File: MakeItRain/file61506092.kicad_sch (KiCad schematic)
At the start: 12 parts, among them Q10 2N7000, Q11 2N7000, Q12 IRF9Z34NPBF

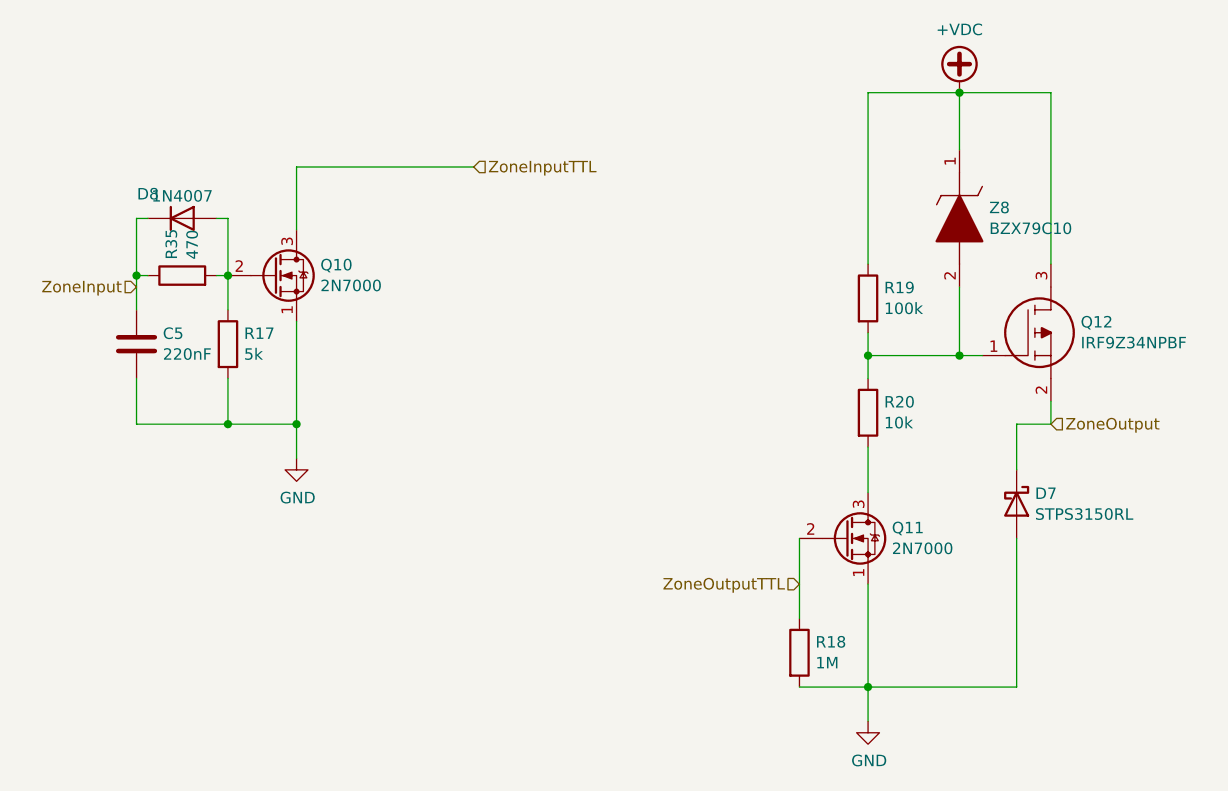
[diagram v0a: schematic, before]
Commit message: upgrading the project to KiCAD 7
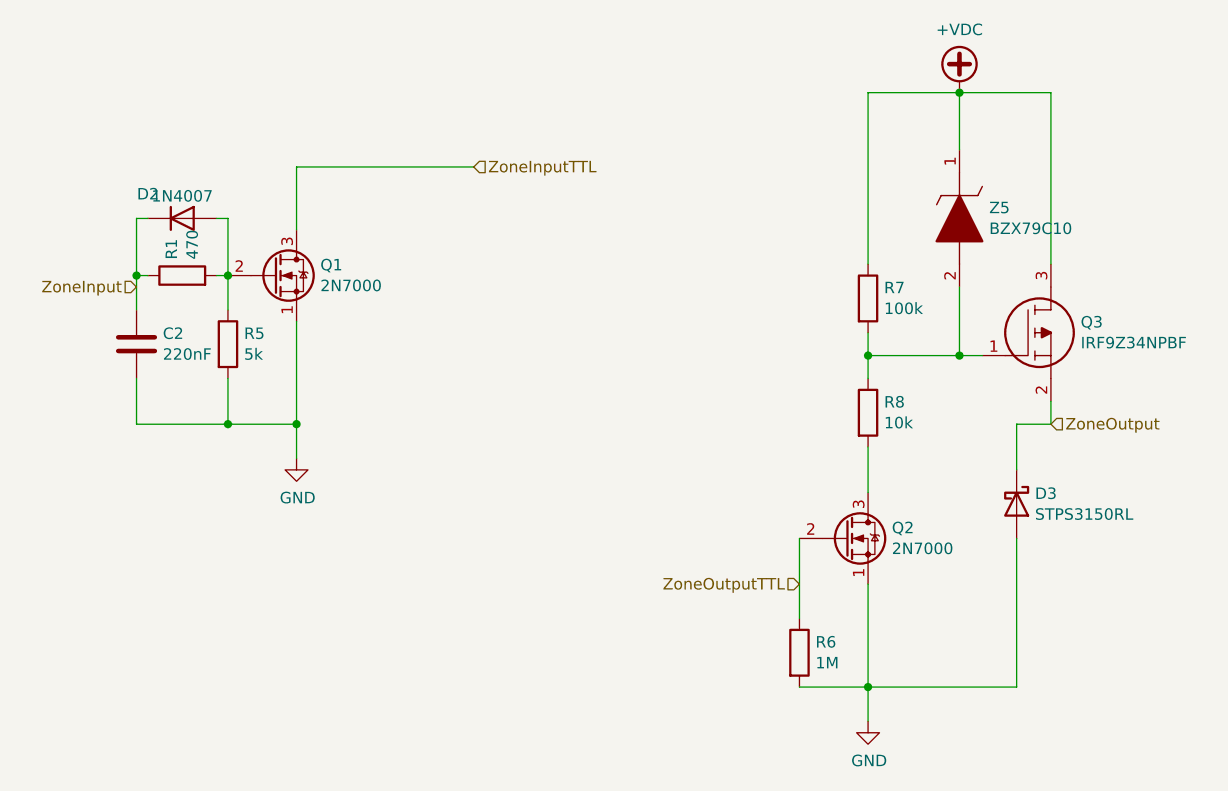
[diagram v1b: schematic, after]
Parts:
- renumbered C5 to C2, D8 to D2, D7 to D3, Q10 to Q1, Q11 to Q2, Q12 to Q3, R35 to R1, R17 to R5, R18 to R6, R19 to R7, R20 to R8, Z8 to Z5

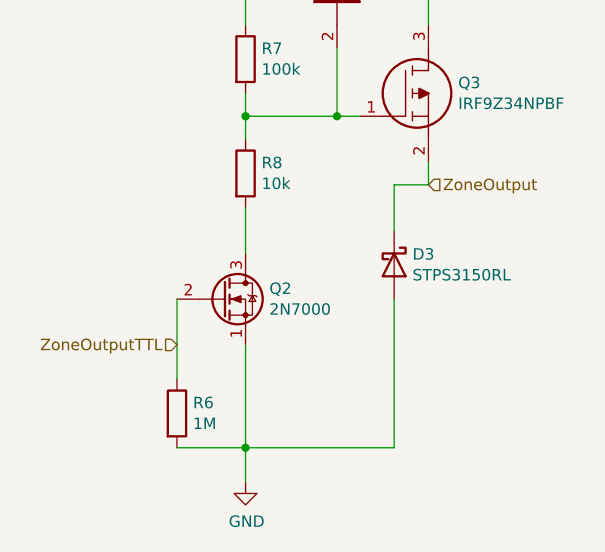
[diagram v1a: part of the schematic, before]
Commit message: WIP - Pre Re-Routing and other Tweaks.
* Removed SMD package for the MCP23008
* removed routings to fix the routes for I2C bus
* flipped rx/tx with SDA/SCL on the expansion port to make routing easier.
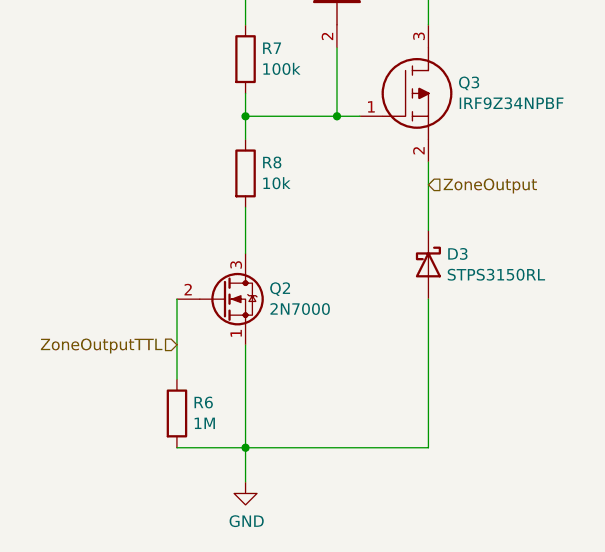
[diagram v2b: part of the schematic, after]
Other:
- moved on the sheet: D3
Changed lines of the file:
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@@
     (stroke (width 0) (type default))
   )
-  (wire (pts (xy 142.24 105.41) (xy 142.24 121.92))
+  (wire (pts (xy 146.05 105.41) (xy 146.05 121.92))
     (stroke (width 0) (type default))
   )
@@
     (stroke (width 0) (type default))
   )
-  (wire (pts (xy 142.24 121.92) (xy 125.73 121.92))
-    (stroke (width 0) (type default))
-  )
-  (wire (pts (xy 142.24 97.79) (xy 142.24 92.71))
+  (wire (pts (xy 146.05 121.92) (xy 125.73 121.92))
     (stroke (width 0) (type default))
   )
@@
     (stroke (width 0) (type default))
   )
-  (wire (pts (xy 142.24 92.71) (xy 146.05 92.71))
-    (stroke (width 0) (type default))
-  )
   (wire (pts (xy 54.61 92.71) (xy 62.23 92.71))
     (stroke (width 0) (type default))
   )
-  (wire (pts (xy 146.05 92.71) (xy 146.05 90.17))
+  (wire (pts (xy 146.05 90.17) (xy 146.05 97.79))
     (stroke (width 0) (type default))
   )
@@
     )
   )
-  (symbol (lib_id "Device:D_Schottky") (at 142.24 101.6 270) (unit 1)
-    (in_bom yes) (on_board yes) (dnp no)
-    (property "Reference" "D3" (at 144.272 100.4316 90)
-      (effects (font (size 1.27 1.27)) (justify left))
-    )
-    (property "Value" "STPS3150RL" (at 144.272 102.743 90)
-      (effects (font (size 1.27 1.27)) (justify left))
-    )
-    (property "Footprint" "Diode_THT:D_DO-201_P15.24mm_Horizontal" (at 142.24 101.6 0)
-      (effects (font (size 1.27 1.27)) hide)
-    )
-    (property "Datasheet" "~" (at 142.24 101.6 0)
-      (effects (font (size 1.27 1.27)) hide)
-    )
+  (symbol (lib_id "Device:D_Schottky") (at 146.05 101.6 270) (unit 1)
+    (in_bom yes) (on_board yes) (dnp no)
+    (property "Reference" "D3" (at 148.082 100.4316 90)
+      (effects (font (size 1.27 1.27)) (justify left))
+    )
+    (property "Value" "STPS3150RL" (at 148.082 102.743 90)
+      (effects (font (size 1.27 1.27)) (justify left))
+    )
+    (property "Footprint" "Diode_THT:D_DO-201_P15.24mm_Horizontal" (at 146.05 101.6 0)
+      (effects (font (size 1.27 1.27)) hide)
+    )
+    (property "Datasheet" "~" (at 146.05 101.6 0)
+      (effects (font (size 1.27 1.27)) hide)
+    )

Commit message: imput redesign
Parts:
- removed C2: 220nF, Capacitor_THT:C_Disc_D5.1mm_W3.2mm_P5.00mm, symbol Device:C
- removed D2: 1N4007, Diode_THT:D_DO-41_SOD81_P10.16mm_Horizontal, symbol Diode:1N4007
- removed Q1: 2N7000, Package_TO_SOT_THT:TO-92_Inline, symbol Transistor_FET:2N7000
- removed R1: 470, Resistor_THT:R_Axial_DIN0207_L6.3mm_D2.5mm_P2.54mm_Vertical, symbol Device:R
- removed R5: 5k, Resistor_THT:R_Axial_DIN0207_L6.3mm_D2.5mm_P2.54mm_Vertical, symbol Device:R
